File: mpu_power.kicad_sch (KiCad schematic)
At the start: 50 parts, among them U401 STM32MP135FAE7

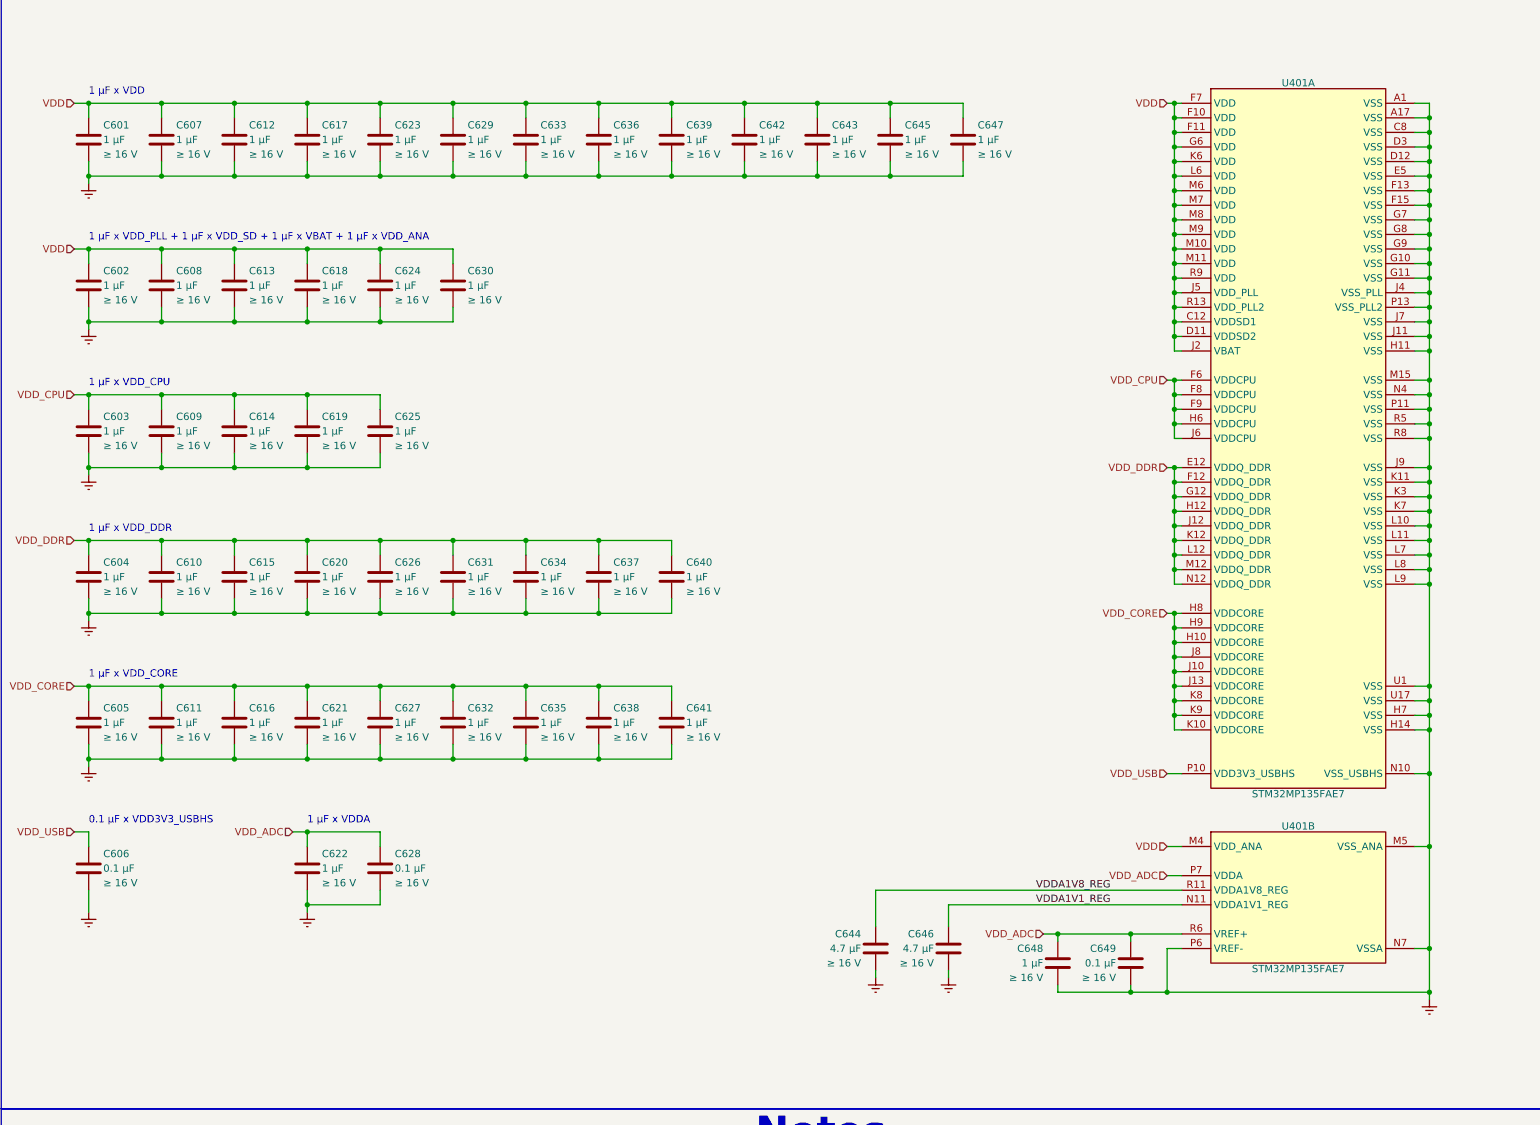
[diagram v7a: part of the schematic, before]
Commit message: Add additional info to passives
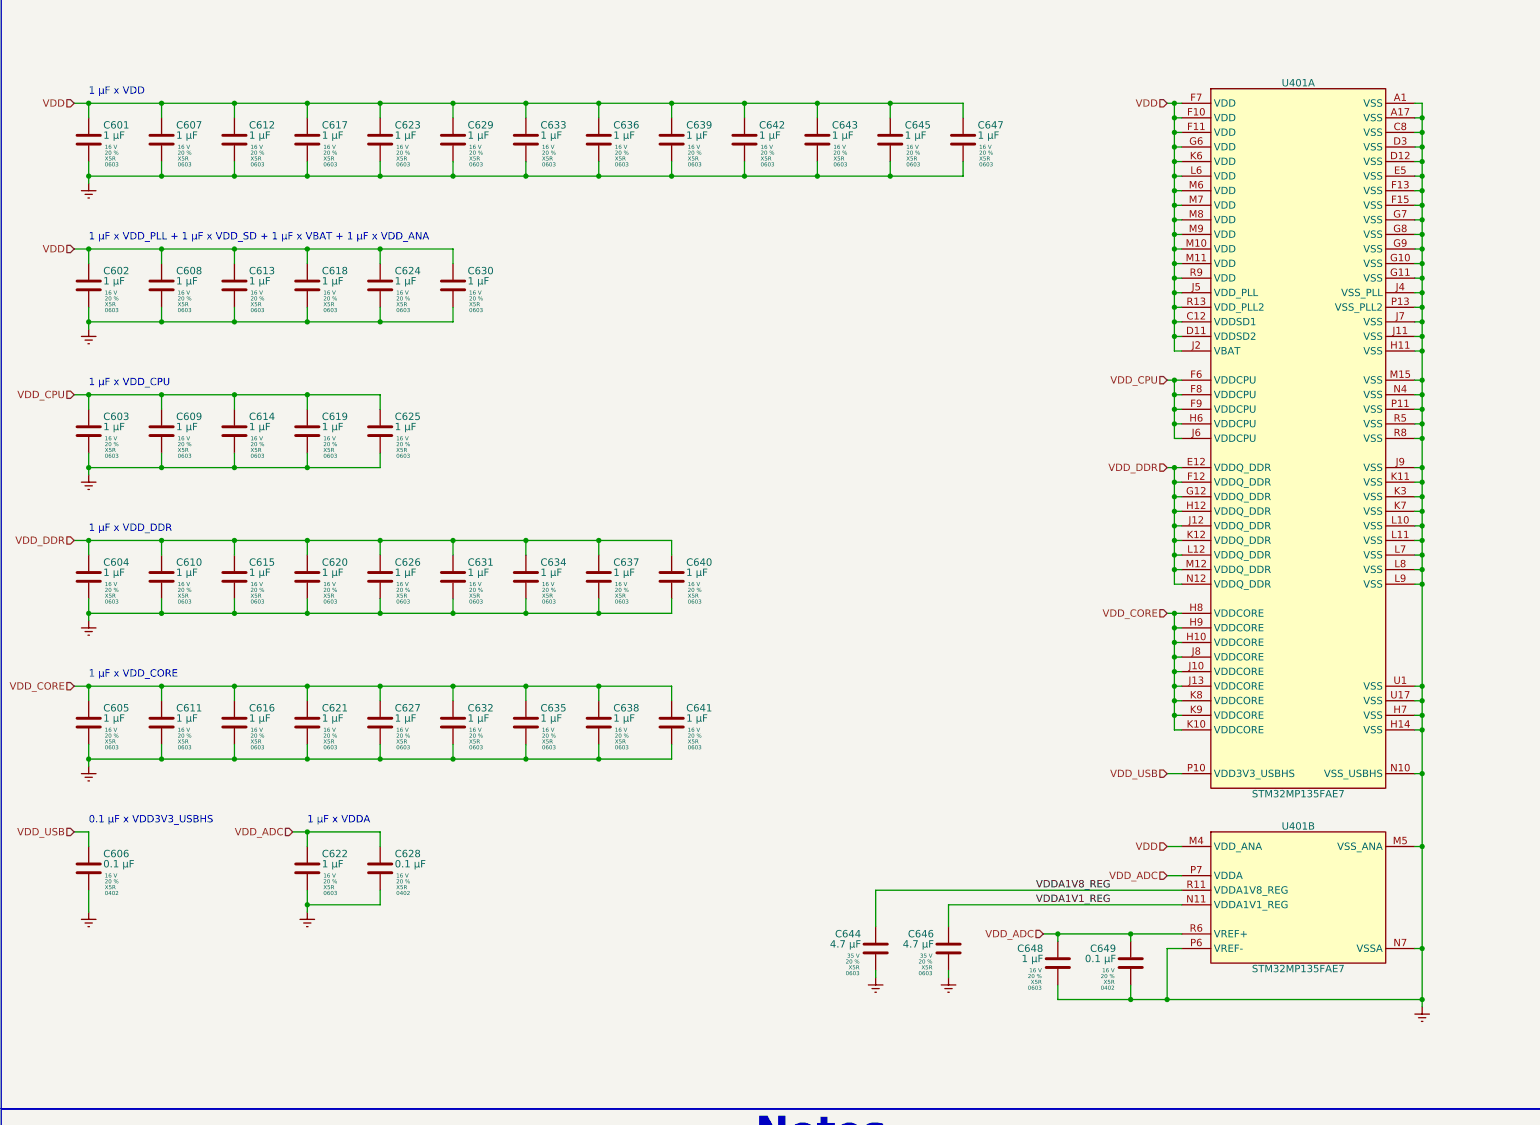
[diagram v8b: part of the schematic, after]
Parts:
- C601, C602, C603, C604, C605, C607, C608, C609, C610, C611, C612, C613, C614, C615, C616, C617, C618, C619, C620, C621, C622, C623, C624, C625, C626, C627, C629, C630, C631, C632, C633, C634, C635, C636, C637, C638, C639, C640, C641, C642, C643, C645, C647, C648: Size (none) -> 0603; Temperature coefficient (none) -> X5R; Tolerance (none) -> 20 %; Voltage rating ≥ 16 V -> 16 V
- C606, C628, C649: Size (none) -> 0402; Temperature coefficient (none) -> X5R; Tolerance (none) -> 20 %; Voltage rating ≥ 16 V -> 16 V
- C644, C646: Size (none) -> 0603; Temperature coefficient (none) -> X5R; Tolerance (none) -> 20 %; Voltage rating ≥ 16 V -> 35 V
- U401: Digi-Key Part Number_1 497-STM32MP135FAE7-ND -> (none); MPN_1 STM32MP135FAE7 -> (none); Manufacturer_1 STMicroelectronics -> (none)
